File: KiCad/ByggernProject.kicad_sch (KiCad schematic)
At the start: 16 parts, among them J1 AVR-JTAG-10, SW1 SW_Push, U1 LATCH, U2 L7805, U3 MAX232, U5 SRAM, U6 ATmega162-16P

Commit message: uPPDADED KEYCAD
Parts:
- added U4: LATCH, symbol 74xx:74LS573
- added U7: ATmega162-16P, Package_DIP:DIP-40_W15.24mm, symbol MCU_Microchip_ATmega:ATmega162-16P
- added U8: SRAM, Package_SO:SOP-28_8.4x18.16mm_P1.27mm, symbol Memory_RAM:HY6264AxJ
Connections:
- new net: U4.12 (Q8), U7.32 (PA7), U8.19 (I/O7)
- new net: U4.13 (Q7), U7.33 (PA6), U8.18 (I/O6)
- new net: U4.14 (Q6), U7.34 (PA5), U8.17 (I/O5)
- new net: U4.15 (Q5), U7.35 (PA4), U8.16 (I/O4)
- new net: U4.16 (Q4), U7.36 (PA3), U8.15 (I/O3)
- new net: U4.17 (Q3), U7.37 (PA2), U8.13 (I/O2)
- new net: U4.18 (Q2), U7.38 (PA1), U8.12 (I/O1)
- new net: U4.19 (Q1), U7.39 (PA0), U8.11 (I/O0)
- new net: U4.2 (D1), U8.10 (A0)
- new net: U4.9 (D8), U8.3 (A7)
- new net: U4.8 (D7), U8.4 (A6)
- new net: U4.7 (D6), U8.5 (A5)
- new net: U4.6 (D5), U8.6 (A4)
- new net: U4.5 (D4), U8.7 (A3)
- new net: U4.4 (D3), U8.8 (A2)
- new net: U4.3 (D2), U8.9 (A1)

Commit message: Added KiCad from KiCadFinalBranch
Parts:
- removed U4: LATCH, symbol 74xx:74LS573
- removed U7: ATmega162-16P, Package_DIP:DIP-40_W15.24mm, symbol MCU_Microchip_ATmega:ATmega162-16P
- removed U8: SRAM, Package_SO:SOP-28_8.4x18.16mm_P1.27mm, symbol Memory_RAM:HY6264AxJ
- added 0.1my, 4.7my1, C7: C, MAX156BCNG_:DIP794W47P254L3213H457Q24, symbol Device:C
- added 1k: R, symbol Device:R
- added ADC1: MAX156BCN, MAX156BCNG_:DIP794W47P254L3213H457Q24, symbol MAX156BCNG_:MAX156BCNG_
- added J2: AVR-JTAG-10, Package_LCC:PLCC-84_29.3x29.3mm_P1.27mm, symbol Connector:AVR-JTAG-10
- added OLED_Controller: (no value), symbol Byggern27:Oled_Controller
- added PC_UART: (no value), symbol Byggern27:PC_UART_Block
- added R2: 1.5k, Package_DIP:DIP-8_W7.62mm, symbol Device:R
- added SW2: SW_Push, Package_DIP:DIP-24_W7.62mm, symbol Switch:SW_Push
- added U7: MAX232, Package_SO:SOIC-8_3.9x4.9mm_P1.27mm, symbol Interface_UART:MAX232
- added U9: ATmega162-16P, Package_DIP:DIP-40_W15.24mm, symbol MCU_Microchip_ATmega:ATmega162-16P
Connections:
- net +5V: now also 0.1my.2, ADC1.20 (REFIN), C7.1, J2.7 (VCC), OLED_Controller. (DISP_RES), U7.16 (VCC), U9.40 (VCC)
- net DXD0: now also U5.21 (A10), U5.23 (A11), U5.24 (A9), U5.25 (A8)
- net GND: now also 0.1my.1, 4.7my1.1, ADC1.12 (DGND), ADC1.21 (AGND), ADC1.4 (VSS), C7.2, J2.10 (GND), J2.2 (GND), OLED_Controller. (DISP_RES), R2.2, SW2.1, U7.15 (GND), U9.20 (GND)
- new net: 1k.2, R2.1
- new net: 4.7my1.2, ADC1.19 (REFOUT)
- new net: ADC.7 (~{WR}), U5.27 (~{WE}), U6.16 (PD6)
- new net: PC_UART. (Rx), U7.4 (R1IN)
- new net: PC_UART. (Rx), U7.5 (T1OUT)
- new net: ADC1.1 (AIN1), OLED_Controller. (DISP_RES)
- new net: ADC1.2 (AIN0), OLED_Controller. (DISP_RES)
- new net: ADC1.23 (AIN3), OLED_Controller. (DISP_RES)
- new net: ADC1.24 (AIN2), OLED_Controller. (DISP_RES)
- new net: ADC1.8 (~{BUSY}), U9.31 (PE0)
- new net: ADC1.9 (CLK), U9.15 (PD5)
- new net: U7.10 ((V-)CS-), U7.16 (VCC)
- new net: U7.11 (C2+(C2-)), U7.15 (GND)
- new net: U7.12 (V-(C2+)), U7.17 (V-)
- new net: U7.2 (T1IN), U9.11 (PD1)
- new net: U7.3 (R1OUT), U9.10 (PD0)
- new net: SW2.2, U9.9 (~{RESET})
- new net: J2.1 (TCK), U9.25 (PC4)
- new net: J2.5 (TMS), U9.26 (PC5)
- new net: J2.3 (TDO), U9.27 (PC6)
- new net: J2.9 (TDI), U9.28 (PC7)
- new net PB6_MISO: OLED_Controller. (DISP_RES)
- new net SRAM Block/PA0: ADC1.18 (D0/A0), U9.39 (PA0)
- new net SRAM Block/PA1: ADC1.17 (D1/A1), U9.38 (PA1)
- new net SRAM Block/PA2: ADC1.16 (D2/A2), U9.37 (PA2)
- new net SRAM Block/PA3: ADC1.15 (D3/PD), U9.36 (PA3)
- new net SRAM Block/PA4: ADC1.14 (D4/INH), U9.35 (PA4)
- new net SRAM Block/PA5: ADC1.13 (D5/BIP), U9.34 (PA5)
- new net SRAM Block/PA6: ADC1.11 (D6/DIFF), U9.33 (PA6)
- new net SRAM Block/PA7: ADC1.10 (D7/*ALL), U9.32 (PA7)
- new net SRAM Block/PC0: U9.21 (PC0)
- new net SRAM Block/PC1: U9.22 (PC1)
- new net SRAM Block/PC2: U9.23 (PC2)
- new net SRAM Block/PC3: ADC1.5 (~{CS}), U9.24 (PC3)
- new net SRAM Block/PD6: ADC1.7 (~{WR}), U9.16 (PD6)
- new net SRAM Block/PD7: ADC1.6 (~{RD}), U9.17 (PD7)
- new net SRAM Block/PE1: U9.30 (PE1)
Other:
- added sheet SRAM Block (sramblock.kicad_sch)
- note added: "AIN0"
- note added: "AIN1"
- note added: "AIN2"
- note added: "AIN3"
- note added: "AINX"
- note added: "PB5 MOSI"
- note added: "PB6 MISO"
- note added: "PB7 SCK"
- note added: "PD2"
- note added: "Pulled Up = D[7:0] is data, Pulled Down = Teansfer data to Command Register. I2C: SA0"
- note added: "RESET = Pulled Up, Chip enable = Pull Down, Connect to MCU"

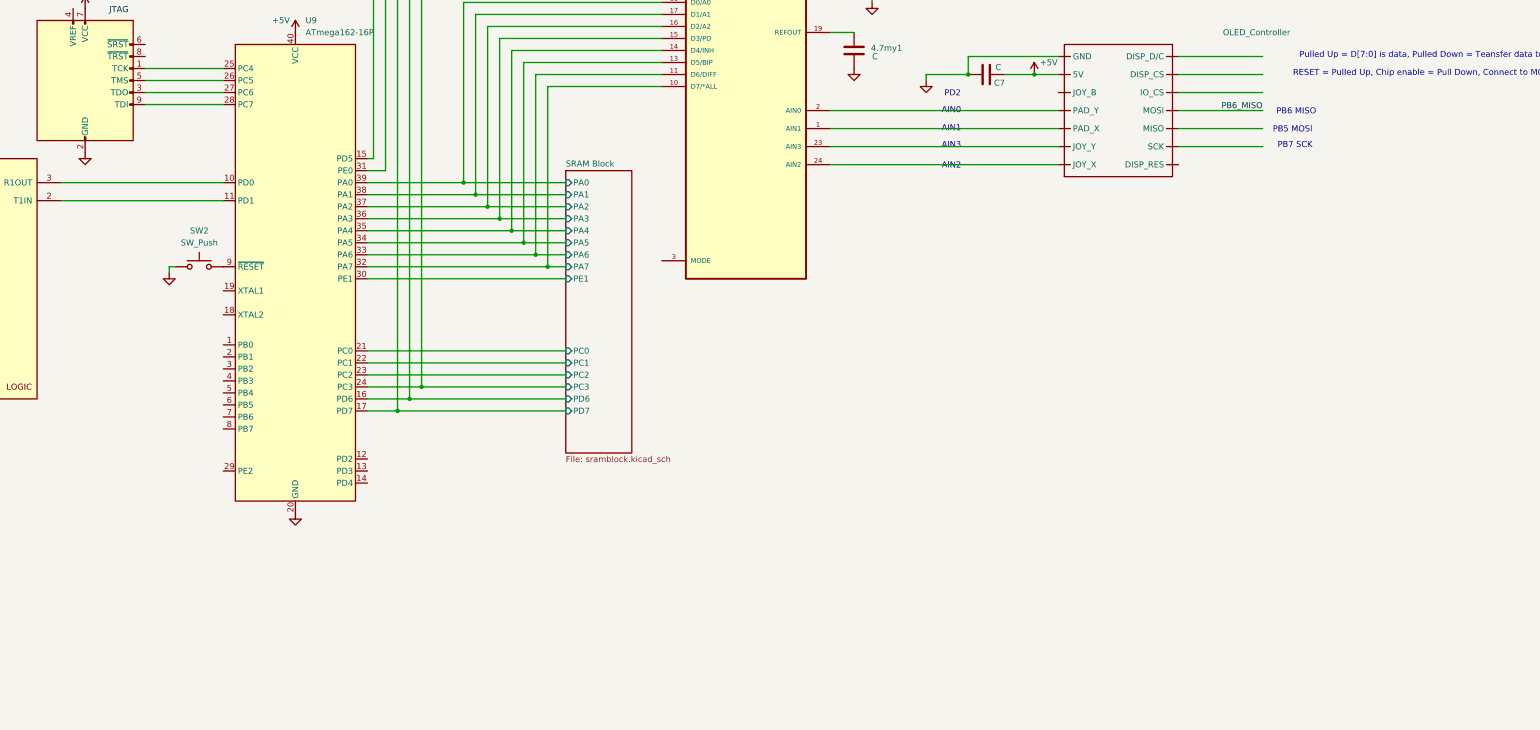
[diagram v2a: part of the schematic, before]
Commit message: KiCad SPI
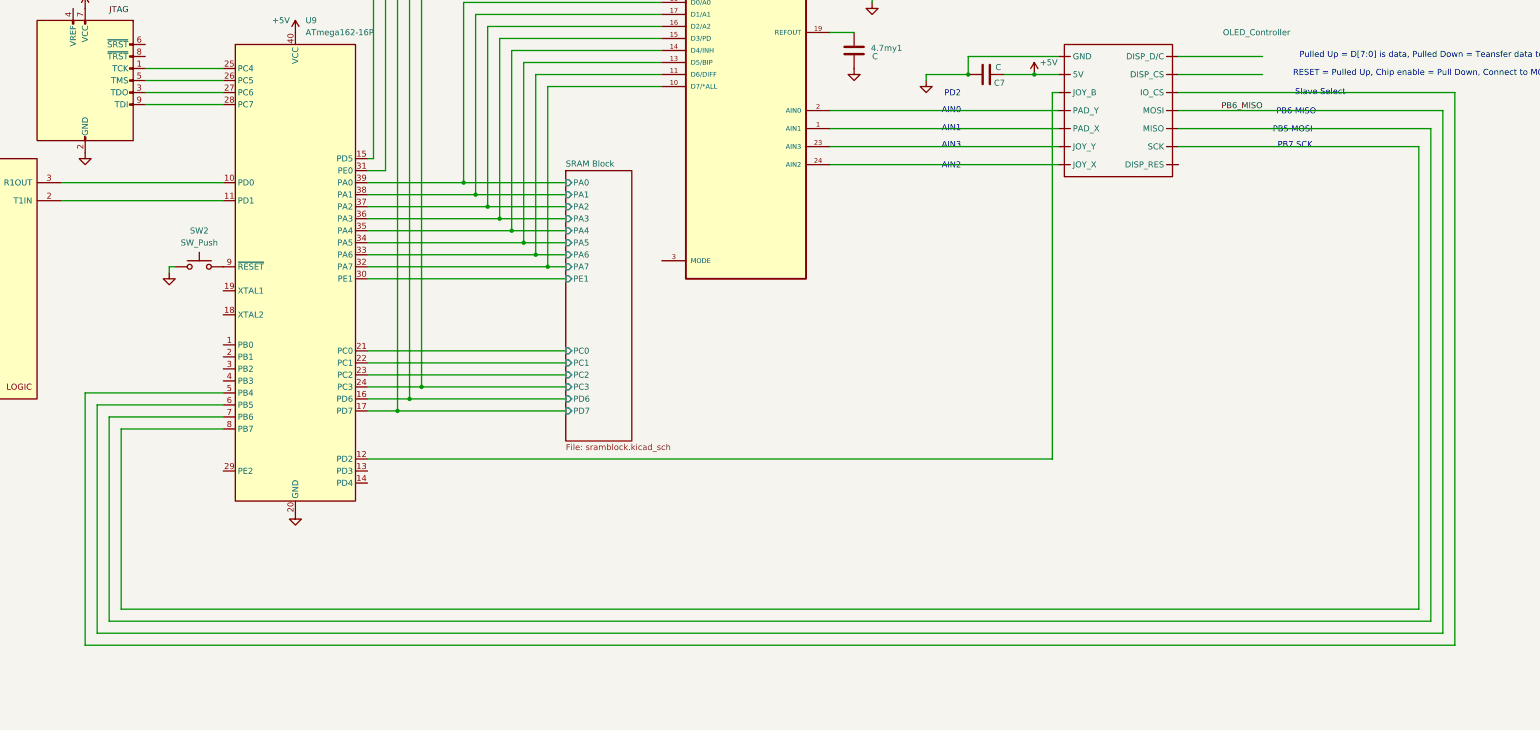
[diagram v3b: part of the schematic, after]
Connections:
- net PB6_MISO: now also U9.6 (PB5)
- net at U9.12 (PD2): now also OLED_Controller. (DISP_RES)
- net at U9.5 (PB4): now also OLED_Controller. (DISP_RES)
- net at U9.7 (PB6): now also OLED_Controller. (DISP_RES)
- net at U9.8 (PB7): now also OLED_Controller. (DISP_RES)
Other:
- note added: "Slave Select"
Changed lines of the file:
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@@
 		)
 	)
+	(text "Slave Select"
+		(exclude_from_sim no)
+		(at 631.952 99.06 0)
+		(effects
+			(font
+				(size 1.27 1.27)
+			)
+		)
+	)
 	(text "PD2"
 		(exclude_from_sim no)
@@
 	(wire
 		(pts
+			(xy 576.58 99.06) (xy 575.31 99.06)
+		)
+		(stroke
+			(width 0)
+			(type default)
+		)
+	)
+	(wire
+		(pts
 			(xy 91.44 560.07) (xy 92.71 560.07)
 		)
@@
 	(wire
 		(pts
+			(xy 378.46 170.18) (xy 400.05 170.18)
+		)
+		(stroke
+			(width 0)
+			(type default)
+		)
+	)
+	(wire
+		(pts
 			(xy 118.11 570.23) (xy 119.38 570.23)
 		)
@@
 	(wire
 		(pts
+			(xy 400.05 167.64) (xy 375.92 167.64)
+		)
+		(stroke
+			(width 0)
+			(type default)
+		)
+	)
+	(wire
+		(pts
 			(xy 36.83 547.37) (xy 38.1 547.37)
 		)
@@
 	(wire
 		(pts
+			(xy 378.46 208.28) (xy 378.46 170.18)
+		)
+		(stroke
+			(width 0)
+			(type default)
+		)
+	)
+	(wire
+		(pts
 			(xy 91.44 552.45) (xy 91.44 554.99)
 		)
@@
 	(wire
 		(pts
+			(xy 430.53 176.53) (xy 575.31 176.53)
+		)
+		(stroke
+			(width 0)
+			(type default)
+		)
+	)
+	(wire
+		(pts
 			(xy 255.27 433.07) (xy 262.89 433.07)
 		)
@@
 	(wire
 		(pts
-			(xy 601.98 102.87) (xy 619.76 102.87)
+			(xy 601.98 102.87) (xy 657.86 102.87)
 		)
 		(stroke
@@
 	(wire
 		(pts
+			(xy 655.32 210.82) (xy 655.32 106.68)
+		)
+		(stroke
+			(width 0)
+			(type default)
+		)
+	)
+	(wire
+		(pts
 			(xy 119.38 538.48) (xy 125.73 538.48)
 		)
@@
 	(wire
 		(pts
+			(xy 375.92 167.64) (xy 375.92 210.82)
+		)
+		(stroke
+			(width 0)
+			(type default)
+		)
+	)
+	(wire
+		(pts
 			(xy 199.39 490.22) (xy 227.33 490.22)
 		)
@@
 	(wire
 		(pts
+			(xy 575.31 99.06) (xy 575.31 176.53)
+		)
+		(stroke
+			(width 0)
+			(type default)
+		)
+	)
+	(wire
+		(pts
 			(xy 36.83 560.07) (xy 38.1 560.07)
 		)
@@
 	(wire
 		(pts
+			(xy 370.84 215.9) (xy 660.4 215.9)
+		)
+		(stroke
+			(width 0)
+			(type default)
+		)
+	)
+	(wire
+		(pts
 			(xy 234.95 558.8) (xy 250.19 558.8)
 		)
@@
 	(wire
 		(pts
+			(xy 660.4 215.9) (xy 660.4 99.06)
+		)
+		(stroke
+			(width 0)
+			(type default)
+		)
+	)
+	(wire
+		(pts
 			(xy 66.04 599.44) (xy 199.39 599.44)
 		)
@@
 	(wire
 		(pts
+			(xy 400.05 162.56) (xy 370.84 162.56)
+		)
+		(stroke
+			(width 0)
+			(type default)
+		)
+	)
+	(wire
+		(pts
 			(xy 238.76 568.96) (xy 238.76 551.18)
 		)
@@
 	(wire
 		(pts
+			(xy 370.84 162.56) (xy 370.84 215.9)
+		)
+		(stroke
+			(width 0)
+			(type default)
+		)
+	)
+	(wire
+		(pts
 			(xy 227.33 482.6) (xy 227.33 490.22)
 		)
@@
 	(wire
 		(pts
+			(xy 373.38 213.36) (xy 657.86 213.36)
+		)
+		(stroke
+			(width 0)
+			(type default)
+		)
+	)
+	(wire
+		(pts
 			(xy 85.09 445.77) (xy 86.36 445.77)
 		)
@@
 	(wire
 		(pts
+			(xy 652.78 208.28) (xy 378.46 208.28)
+		)
+		(stroke
+			(width 0)
+			(type default)
+		)
+	)
+	(wire
+		(pts
 			(xy 537.21 73.66) (xy 537.21 72.39)
 		)
@@
 	(wire
 		(pts
+			(xy 652.78 110.49) (xy 652.78 208.28)
+		)
+		(stroke
+			(width 0)
+			(type default)
+		)
+	)
+	(wire
+		(pts
 			(xy 436.88 64.77) (xy 492.76 64.77)
 		)
@@
 	(wire
 		(pts
+			(xy 375.92 210.82) (xy 655.32 210.82)
+		)
+		(stroke
+			(width 0)
+			(type default)
+		)
+	)
+	(wire
+		(pts
 			(xy 208.28 471.17) (xy 218.44 471.17)
 		)
@@
 	(wire
 		(pts
+			(xy 657.86 213.36) (xy 657.86 102.87)
+		)
+		(stroke
+			(width 0)
+			(type default)
+		)
+	)
+	(wire
+		(pts
 			(xy 121.92 491.49) (xy 124.46 491.49)
 		)
@@
 	(wire
 		(pts
-			(xy 601.98 110.49) (xy 619.76 110.49)
+			(xy 601.98 110.49) (xy 652.78 110.49)
 		)
 		(stroke
@@
 	(wire
 		(pts
-			(xy 601.98 99.06) (xy 619.76 99.06)
+			(xy 601.98 99.06) (xy 660.4 99.06)
 		)
 		(stroke
@@
 	(wire
 		(pts
+			(xy 373.38 165.1) (xy 373.38 213.36)
+		)
+		(stroke
+			(width 0)
+			(type default)
+		)
+	)
+	(wire
+		(pts
 			(xy 388.62 135.89) (xy 388.62 137.16)
 		)
@@
 	(wire
 		(pts
+			(xy 400.05 165.1) (xy 373.38 165.1)
+		)
+		(stroke
+			(width 0)
+			(type default)
+		)
+	)
+	(wire
+		(pts
 			(xy 217.17 520.7) (xy 217.17 518.16)
 		)
@@
 	(wire
 		(pts
-			(xy 601.98 106.68) (xy 619.76 106.68)
+			(xy 601.98 106.68) (xy 655.32 106.68)
 		)
 		(stroke
@@
 	(sheet
 		(at 472.44 115.57)
-		(size 13.97 59.69)
+		(size 13.97 57.15)
 		(exclude_from_sim no)
 		(in_bom yes)
@@
 		)
 		(property "Sheetfile" "sramblock.kicad_sch"
-			(at 472.44 175.8446 0)
+			(at 472.44 173.3046 0)
 			(show_name no)
 			(do_not_autoplace no)
